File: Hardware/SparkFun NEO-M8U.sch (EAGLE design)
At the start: 50 parts, among them J13 U.FL, J2 Qwiic Right Angle, J4 Qwiic Right Angle, U2 3.3V

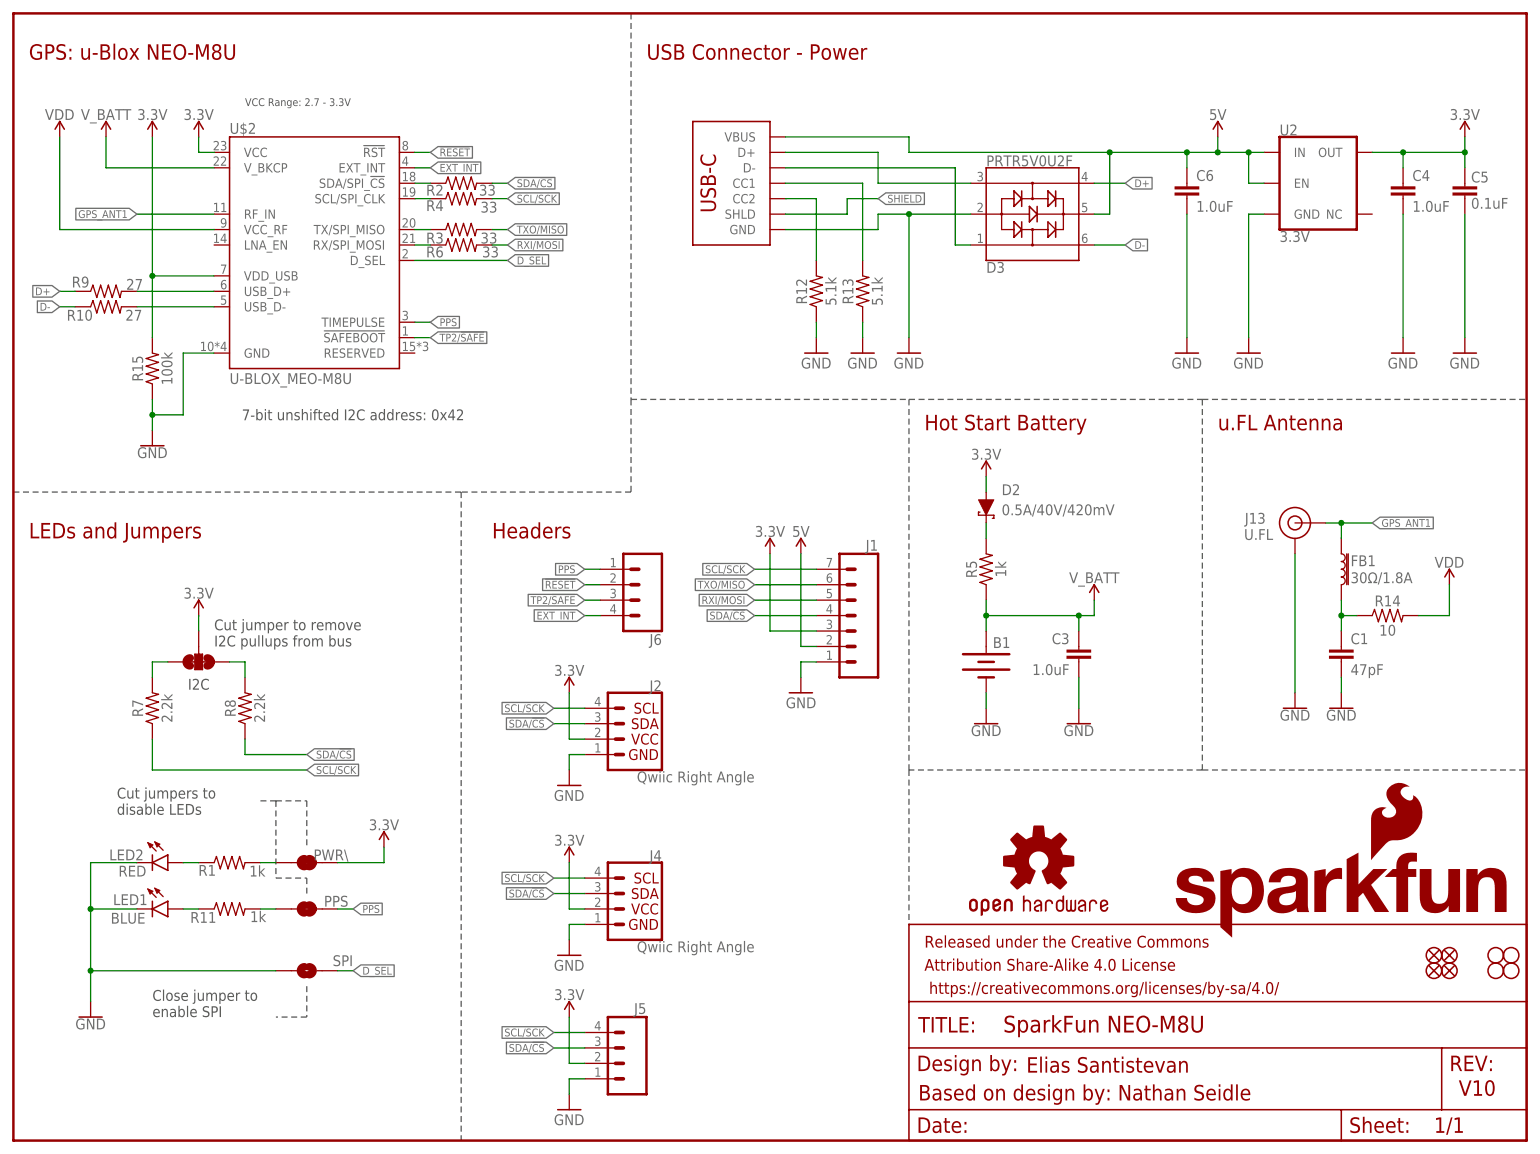
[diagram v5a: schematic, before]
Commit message: Removes old gerbers and buzzard labels, fixes some minor board inconsistencies
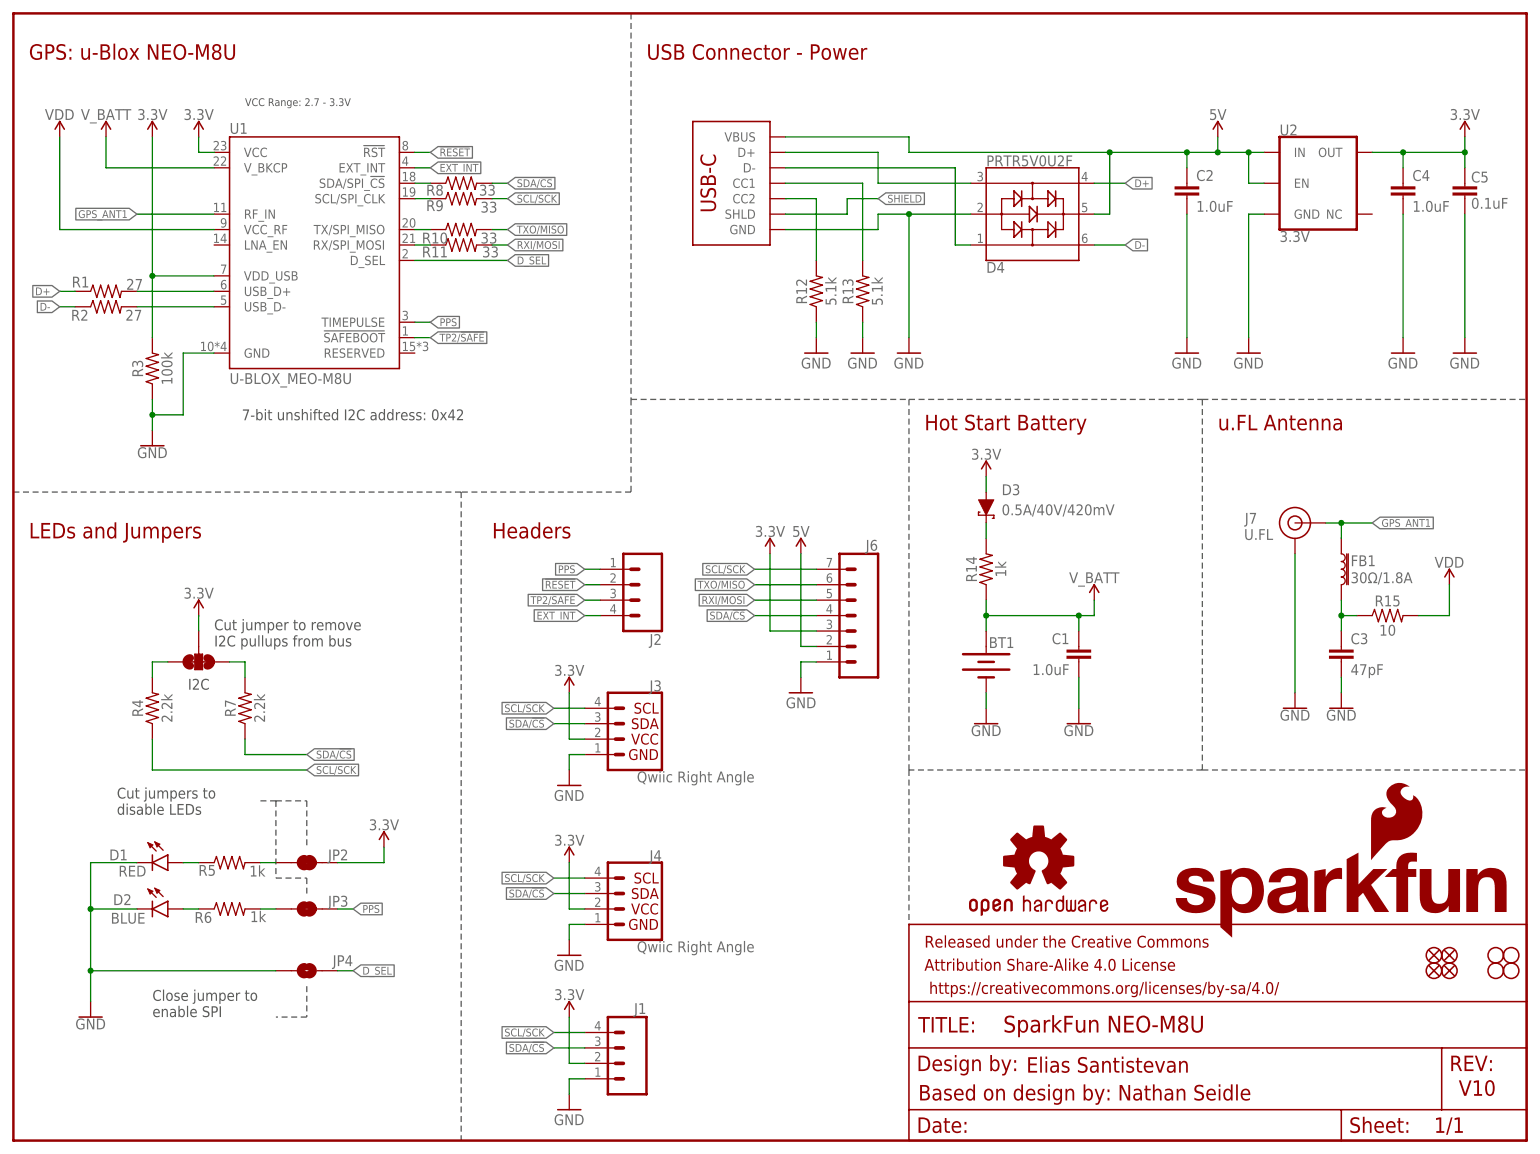
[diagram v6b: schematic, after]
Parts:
- removed JP21: FIDUCIALUFIDUCIAL, SparkFun:FIDUCIALUFIDUCIAL
- removed LED1: BLUE, SparkFun-LED:LED-BLUE0603
- added D4: PRTR5V0U2F, SparkFun-IC-Power:PRTR5V0U2F
- added JP1: JUMPER-SMT_3_2-NC_TRACE_SILK, SparkFun-Jumpers:JUMPER-SMT_3_2-NC_TRACE_SILK
- C1: value 47pF -> 1.0uF; device SparkFun-Capacitors:47PF-0603-50V-5% -> SparkFun-Capacitors:1.0UF-0603-16V-10%
- C3: value 1.0uF -> 47pF; device SparkFun-Capacitors:1.0UF-0603-16V-10% -> SparkFun-Capacitors:47PF-0603-50V-5%
- D2: value 0.5A/40V/420mV -> BLUE; device SparkFun-DiscreteSemi:DIODE-SCHOTTKY-PMEG4005EJ -> SparkFun-LED:LED-BLUE0603
- D3: value PRTR5V0U2F -> 0.5A/40V/420mV; device SparkFun-IC-Power:PRTR5V0U2F -> SparkFun-DiscreteSemi:DIODE-SCHOTTKY-PMEG4005EJ
- J1: device SparkFun-Connectors:CONN_07NO_SILK -> SparkFun-Connectors:CONN_041X04_NO_SILK
- J2: value Qwiic Right Angle -> (none); device SparkFun-Connectors:I2C_STANDARDQWIIC -> SparkFun-Connectors:CONN_041X04_NO_SILK
- J3: value (none) -> Qwiic Right Angle; device SparkFun-Connectors:USB_C_2-LAYER_PADS -> SparkFun-Connectors:I2C_STANDARDQWIIC
- J5: device SparkFun-Connectors:CONN_041X04_NO_SILK -> SparkFun-Connectors:USB_C_2-LAYER_PADS
- J6: device SparkFun-Connectors:CONN_041X04_NO_SILK -> SparkFun-Connectors:CONN_07NO_SILK
- JP5: value JUMPER-SMT_3_2-NC_TRACE_SILK -> FIDUCIALUFIDUCIAL; device SparkFun-Jumpers:JUMPER-SMT_3_2-NC_TRACE_SILK -> SparkFun:FIDUCIALUFIDUCIAL
- R1: value 1k -> 27; device SparkFun-Resistors:1KOHM-0603-1/10W-1% -> SparkFun-Resistors:27OHM-0603-1/10W-1%
- R10, R9: value 27 -> 33; device SparkFun-Resistors:27OHM-0603-1/10W-1% -> SparkFun-Resistors:33OHM-0603-1/10W-1%
- R11: value 1k -> 33; device SparkFun-Resistors:1KOHM-0603-1/10W-1% -> SparkFun-Resistors:33OHM-0603-1/10W-1%
- R14: value 10 -> 1k; device SparkFun-Resistors:10OHM-0603-1/10W-1% -> SparkFun-Resistors:1KOHM-0603-1/10W-1%
- R15: value 100k -> 10; device SparkFun-Resistors:100KOHM-0603-1/10W-1% -> SparkFun-Resistors:10OHM-0603-1/10W-1%
- R2: value 33 -> 27; device SparkFun-Resistors:33OHM-0603-1/10W-1% -> SparkFun-Resistors:27OHM-0603-1/10W-1%
- R3: value 33 -> 100k; device SparkFun-Resistors:33OHM-0603-1/10W-1% -> SparkFun-Resistors:100KOHM-0603-1/10W-1%
- R4: value 33 -> 2.2k; device SparkFun-Resistors:33OHM-0603-1/10W-1% -> SparkFun-Resistors:2.2KOHM-0603-1/10W-1%
- R6: value 33 -> 1k; device SparkFun-Resistors:33OHM-0603-1/10W-1% -> SparkFun-Resistors:1KOHM-0603-1/10W-1%
- R8: value 2.2k -> 33; device SparkFun-Resistors:2.2KOHM-0603-1/10W-1% -> SparkFun-Resistors:33OHM-0603-1/10W-1%
- renumbered B1 to BT1, C6 to C2, J13 to J7, JP101 to JP10, JP31 to JP11, JP41 to JP12, JP61 to JP7, JP71 to JP6, JP81 to JP8, JP91 to JP9, LED2 to D1, PPS to JP3, PWR\ to JP2, SPI to JP4, U$2 to U1
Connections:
- net !RESET: now also J2.2; no longer J6.2
- net 3.3V: now also D3.A, J1.2, J3.2, J6.3, JP1.2, R3.2; no longer D2.A, J1.3, J2.2, J5.2, JP5.2, R15.2
- net 5V: now also D4.5, J5.VBUS, J6.2; no longer D3.5, J1.2, J3.VBUS
- net ANT_VCC: now also C3.1, R15.1; no longer C1.1, R14.1
- net D+: now also D4.4, R1.1; no longer D3.4, R9.1
- net D-: now also D4.6, R2.1; no longer D3.6, R10.1
- net EXT_INT: now also J2.4; no longer J6.4
- net GND: now also D2.C, D4.2, J3.1, J5.GND, J6.1, R3.1; no longer D3.2, J2.1, J3.GND, J5.1, LED1.C, R15.1
- net N$1: now also R5.2; no longer R1.2
- net N$10: now also R5.1; no longer R1.1
- net N$11: now also R1.2; no longer R9.2
- net N$12: now also R2.2; no longer R10.2
- net N$13: now also R9.1; no longer R4.1
- net N$15: now also R10.1; no longer R3.1
- net N$16: now also R11.1; no longer R6.1
- net N$2: now also D2.A, R6.1; no longer LED1.A, R11.1
- net N$3: now also R8.1; no longer R2.1
- net N$4: now also R6.2; no longer R11.2
- net N$5: now also JP1.1, R7.2; no longer JP5.1, R8.2
- net N$6: now also D3.C, R14.2; no longer D2.C, R5.2
- net N$7: now also J5.CC2; no longer J3.CC2
- net N$8: now also JP1.3, R4.2; no longer JP5.3, R7.2
- net N$9: now also J5.CC1; no longer J3.CC1
- net PPS: now also J2.1; no longer J6.1
- net RXI/MOSI: now also J6.5, R11.2; no longer J1.5, R6.2
- net SCL/SCK: now also J1.4, J3.4, J6.7, R4.1, R9.2; no longer J1.7, J2.4, J5.4, R4.2, R7.1
- net SDA/!CS: now also J1.3, J3.3, J6.4, R7.1, R8.2; no longer J1.4, J2.3, J5.3, R2.2, R8.1
- net SHIELD: now also J5.SHLD; no longer J3.SHLD
- net TP2/!SAFE: now also J2.3; no longer J6.3
- net TXO/MISO: now also J6.6, R10.2; no longer J1.6, R3.2
- net USB_D+: now also D4.3, J5.D+; no longer D3.3, J3.D+
- net USB_D-: now also D4.1, J5.D-; no longer D3.1, J3.D-
- net VDD: now also R15.2; no longer R14.2
- net V_BATT: now also C1.1, R14.1; no longer C3.1, R5.1
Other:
- moved on the sheet: C1, C3, R1, R10, R11, R14, R15, R2, R3, R4, R5, R6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

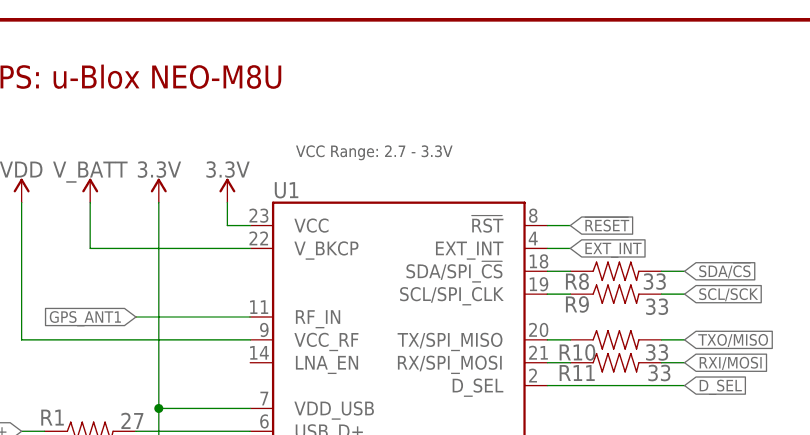
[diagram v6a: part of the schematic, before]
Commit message: Adjusts some wonky trace widths, moves some traces for better pour
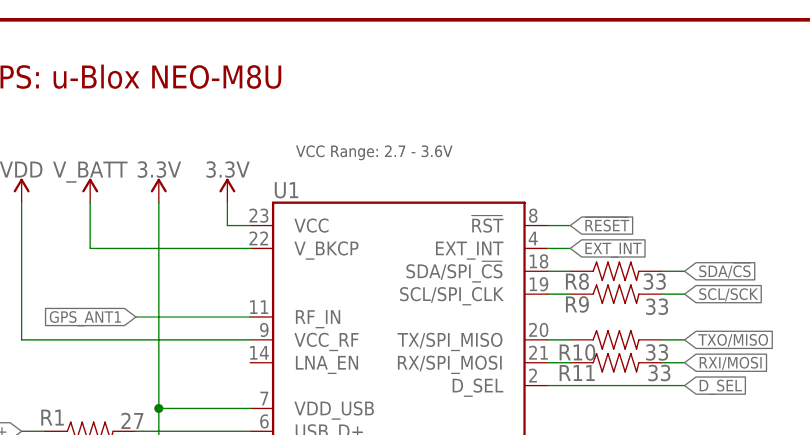
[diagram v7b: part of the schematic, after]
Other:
- note added: "VCC Range: 2.7 - 3.6V"
- note removed: "VCC Range: 2.7 - 3.3V"
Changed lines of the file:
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@@
 <text x="104.14" y="177.8" size="2.54" layer="94" font="vector">USB Connector - Power</text>
 <text x="148.844" y="6.604" size="2.54" layer="94" font="vector">Based on design by: Nathan Seidle</text>
-<text x="38.1" y="170.18" size="1.27" layer="97" font="vector">VCC Range: 2.7 - 3.3V</text>
+<text x="38.1" y="170.18" size="1.27" layer="97" font="vector">VCC Range: 2.7 - 3.6V</text>
 <wire x1="43.18" y1="55.88" x2="43.18" y2="43.18" width="0.2032" layer="97" style="dashdot"/>
 <wire x1="48.26" y1="25.4" x2="48.26" y2="20.32" width="0.2032" layer="97" style="dashdot"/>

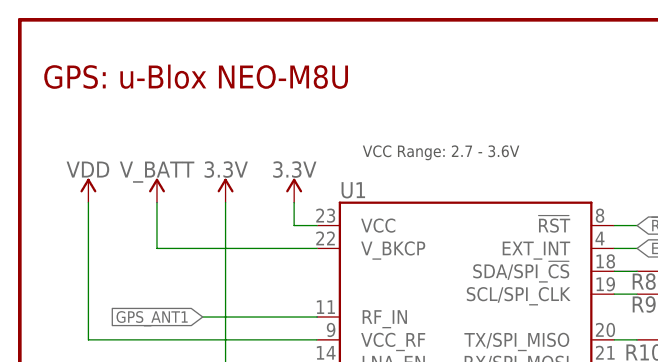
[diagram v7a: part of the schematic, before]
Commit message: Fixes "u-blox" typo in schematic
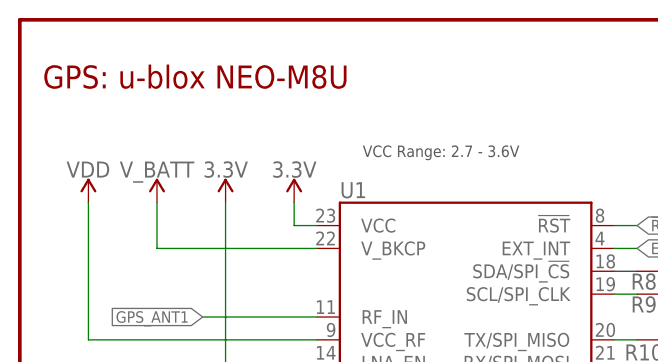
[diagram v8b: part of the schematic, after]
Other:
- note added: "GPS: u-blox NEO-M8U"
- note removed: "GPS: u-Blox NEO-M8U"
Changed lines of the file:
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@@
 <?xml version="1.0" encoding="utf-8"?>
 <!DOCTYPE eagle SYSTEM "eagle.dtd">
-<eagle version="9.5.2">
+<eagle version="9.6.2">
 <drawing>
 <settings>
@@
 <text x="2.54" y="99.06" size="2.54" layer="94" font="vector">LEDs and Jumpers</text>
 <text x="149.86" y="116.84" size="2.54" layer="94" font="vector">Hot Start Battery</text>
-<text x="2.54" y="177.8" size="2.54" layer="94" font="vector">GPS: u-Blox NEO-M8U</text>
+<text x="2.54" y="177.8" size="2.54" layer="94" font="vector">GPS: u-blox NEO-M8U</text>
 <wire x1="73.66" y1="106.68" x2="73.66" y2="0" width="0.1524" layer="97" style="shortdash"/>
 <wire x1="40.64" y1="55.88" x2="43.18" y2="55.88" width="0.2032" layer="97" style="dashdot"/>
